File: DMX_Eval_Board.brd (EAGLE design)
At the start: 80 x 75 mm, 11 parts, among them X1 NC3FAH2, X2 NC3MBH-B

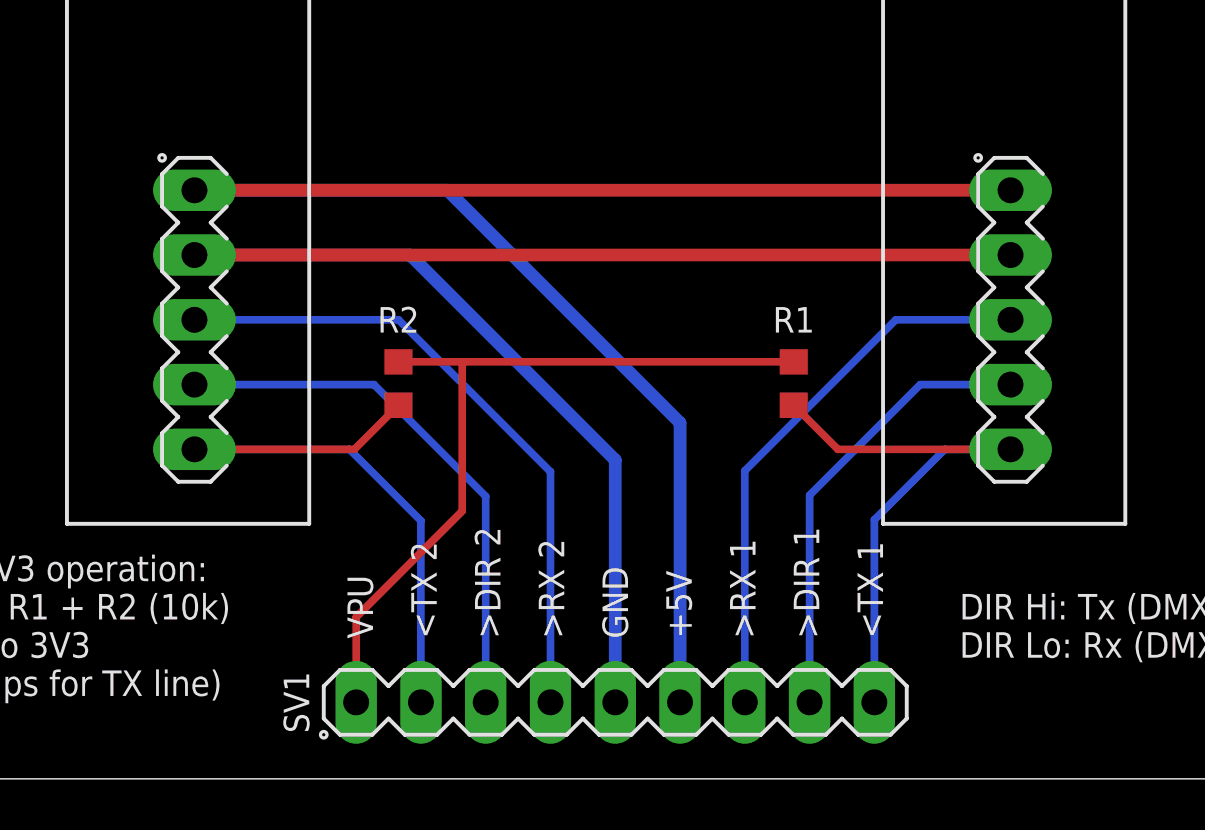
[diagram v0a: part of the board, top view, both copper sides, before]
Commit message: Updated spacing between pin headers to be within a 0.1" grid - This way it is breadboard compatible
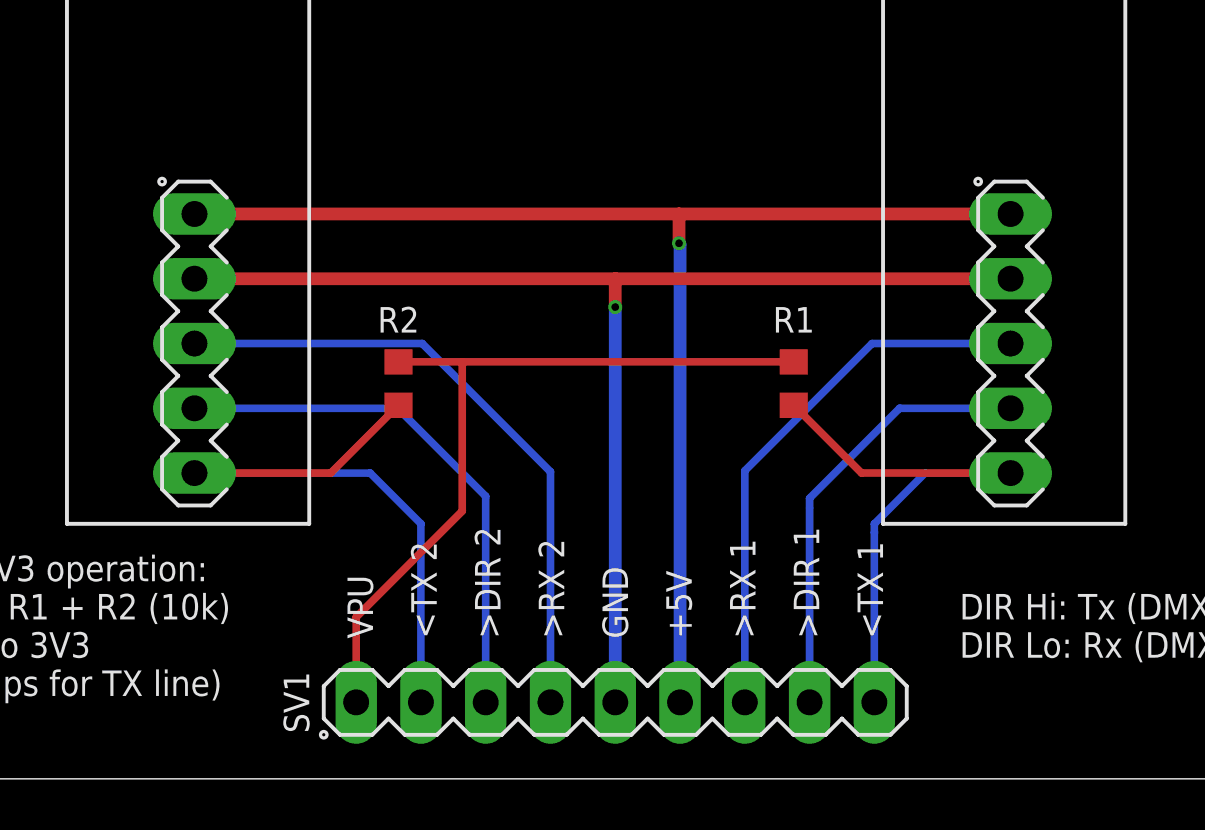
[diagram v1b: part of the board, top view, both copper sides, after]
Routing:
- net +5V: track 65.8 -> 51.2 mm, vias 0 -> 1
- net GND: track 61.3 -> 48.6 mm, vias 0 -> 1
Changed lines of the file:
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@@
 <contactref element="MOD1" pad="2"/>
 <contactref element="MOD2" pad="2"/>
-<wire x1="24" y1="20.54" x2="56" y2="20.54" width="0.5" layer="1"/>
-<wire x1="32.46" y1="20.54" x2="24" y2="20.54" width="0.5" layer="16"/>
+<wire x1="24" y1="19.61" x2="40.5" y2="19.61" width="0.5" layer="1"/>
 <contactref element="SV1" pad="5"/>
-<wire x1="40.5" y1="3" x2="40.5" y2="12.5" width="0.5" layer="16"/>
-<wire x1="40.5" y1="12.5" x2="32.46" y2="20.54" width="0.5" layer="16"/>
+<wire x1="40.5" y1="19.61" x2="56" y2="19.61" width="0.5" layer="1"/>
+<via x="40.5" y="18.5" extent="1-16" drill="0.3"/>
+<wire x1="40.5" y1="18.5" x2="40.5" y2="19.61" width="0.5" layer="1"/>
+<wire x1="40.5" y1="3" x2="40.5" y2="18.5" width="0.5" layer="16"/>
 </signal>
 <signal name="+5V">
 <contactref element="MOD2" pad="1"/>
 <contactref element="MOD1" pad="1"/>
-<wire x1="24" y1="23.08" x2="56" y2="23.08" width="0.5" layer="1"/>
-<wire x1="33.92" y1="23.08" x2="24" y2="23.08" width="0.5" layer="16"/>
+<wire x1="24" y1="22.15" x2="43" y2="22.15" width="0.5" layer="1"/>
 <contactref element="SV1" pad="6"/>
-<wire x1="43.04" y1="3" x2="43.04" y2="13.96" width="0.5" layer="16"/>
-<wire x1="43.04" y1="13.96" x2="33.92" y2="23.08" width="0.5" layer="16"/>
+<wire x1="43" y1="22.15" x2="56" y2="22.15" width="0.5" layer="1"/>
+<wire x1="43.04" y1="20.96" x2="43" y2="21" width="0.5" layer="16"/>
+<via x="43" y="21" extent="1-16" drill="0.3"/>
+<wire x1="43" y1="21" x2="43" y2="22.15" width="0.5" layer="1"/>
+<wire x1="43.04" y1="3" x2="43.04" y2="20.96" width="0.5" layer="16"/>
 </signal>
 <signal name="TX_2">
@@
 <contactref element="SV1" pad="2"/>
 <contactref element="R2" pad="1"/>
-<wire x1="30.08" y1="12.92" x2="24" y2="12.92" width="0.3" layer="16"/>
-<wire x1="32.88" y1="3" x2="32.88" y2="10.12" width="0.3" layer="16"/>
-<wire x1="32.88" y1="10.12" x2="30.08" y2="12.92" width="0.3" layer="16"/>
-<wire x1="24" y1="12.92" x2="30.27" y2="12.92" width="0.3" layer="1"/>
-<wire x1="30.27" y1="12.92" x2="32" y2="14.65" width="0.3" layer="1"/>
+<wire x1="32.88" y1="3" x2="32.88" y2="10" width="0.3" layer="16"/>
+<wire x1="32.88" y1="10" x2="30.89" y2="11.99" width="0.3" layer="16"/>
+<wire x1="30.89" y1="11.99" x2="24" y2="11.99" width="0.3" layer="16"/>
+<wire x1="32" y1="14.65" x2="29.34" y2="11.99" width="0.3" layer="1"/>
+<wire x1="29.34" y1="11.99" x2="24" y2="11.99" width="0.3" layer="1"/>
 </signal>
 <signal name="N$8">
 <contactref element="MOD2" pad="4"/>
 <contactref element="SV1" pad="3"/>
-<wire x1="31.04" y1="15.46" x2="24" y2="15.46" width="0.3" layer="16"/>
 <wire x1="35.42" y1="3" x2="35.42" y2="11.08" width="0.3" layer="16"/>
-<wire x1="35.42" y1="11.08" x2="31.04" y2="15.46" width="0.3" layer="16"/>
+<wire x1="35.42" y1="11.08" x2="31.97" y2="14.53" width="0.3" layer="16"/>
+<wire x1="31.97" y1="14.53" x2="24" y2="14.53" width="0.3" layer="16"/>
 </signal>
 <signal name="N$9">
 <contactref element="MOD2" pad="3"/>
 <contactref element="SV1" pad="4"/>
-<wire x1="32" y1="18" x2="24" y2="18" width="0.3" layer="16"/>
 <wire x1="37.96" y1="3" x2="37.96" y2="12.04" width="0.3" layer="16"/>
-<wire x1="37.96" y1="12.04" x2="32" y2="18" width="0.3" layer="16"/>
+<wire x1="37.96" y1="12.04" x2="32.93" y2="17.07" width="0.3" layer="16"/>
+<wire x1="32.93" y1="17.07" x2="24" y2="17.07" width="0.3" layer="16"/>
 </signal>
 <signal name="TX_1">
@@
 <contactref element="SV1" pad="9"/>
 <contactref element="R1" pad="1"/>
-<wire x1="50.66" y1="3" x2="50.66" y2="10.16" width="0.3" layer="16"/>
-<wire x1="56" y1="12.92" x2="53.42" y2="12.92" width="0.3" layer="16"/>
-<wire x1="53.42" y1="12.92" x2="50.66" y2="10.16" width="0.3" layer="16"/>
-<wire x1="56" y1="12.92" x2="49.23" y2="12.92" width="0.3" layer="1"/>
-<wire x1="49.23" y1="12.92" x2="47.5" y2="14.65" width="0.3" layer="1"/>
+<wire x1="50.66" y1="3" x2="50.66" y2="9.66" width="0.3" layer="16"/>
+<wire x1="50.66" y1="10" x2="50.66" y2="9.66" width="0.3" layer="16"/>
+<wire x1="50.66" y1="10" x2="52.65" y2="11.99" width="0.3" layer="16"/>
+<wire x1="52.65" y1="11.99" x2="56" y2="11.99" width="0.3" layer="16"/>
+<wire x1="50.16" y1="11.99" x2="56" y2="11.99" width="0.3" layer="1"/>
+<wire x1="47.5" y1="14.65" x2="50.16" y2="11.99" width="0.3" layer="1"/>
 </signal>
 <signal name="N$11">
 <contactref element="MOD1" pad="4"/>
 <contactref element="SV1" pad="8"/>
-<wire x1="48.12" y1="3" x2="48.12" y2="11.12" width="0.3" layer="16"/>
-<wire x1="56" y1="15.46" x2="52.46" y2="15.46" width="0.3" layer="16"/>
-<wire x1="52.46" y1="15.46" x2="48.12" y2="11.12" width="0.3" layer="16"/>
+<wire x1="48.12" y1="3" x2="48.12" y2="10.62" width="0.3" layer="16"/>
+<wire x1="48.12" y1="11" x2="48.12" y2="10.62" width="0.3" layer="16"/>
+<wire x1="48.12" y1="11" x2="51.65" y2="14.53" width="0.3" layer="16"/>
+<wire x1="51.65" y1="14.53" x2="56" y2="14.53" width="0.3" layer="16"/>
 </signal>
 <signal name="N$12">
@@
 <contactref element="SV1" pad="7"/>
 <wire x1="45.58" y1="3" x2="45.58" y2="12.08" width="0.3" layer="16"/>
-<wire x1="56" y1="18" x2="51.5" y2="18" width="0.3" layer="16"/>
-<wire x1="51.5" y1="18" x2="45.58" y2="12.08" width="0.3" layer="16"/>
+<wire x1="45.58" y1="12.08" x2="50.57" y2="17.07" width="0.3" layer="16"/>
+<wire x1="50.57" y1="17.07" x2="56" y2="17.07" width="0.3" layer="16"/>
 </signal>
 <signal name="VPU">
